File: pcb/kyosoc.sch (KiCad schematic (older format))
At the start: 134 parts, among them J1 USB_C_Receptacle, SW1 SW_Push, SW10 SW_Push, SW11 SW_Push, SW12 SW_Push, SW13 SW_Push, SW14 SW_Push, SW15 SW_Push, SW16 SW_Push, SW17 SW_Push, SW18 SW_Push, SW19 SW_Push, SW2 SW_Push, SW20 SW_Push, SW21 SW_Push, SW22 SW_Push, SW23 SW_Push, SW24 SW_Push, SW25 SW_Push, SW26 SW_Push, SW27 SW_Push, SW28 SW_Push, SW29 SW_Push, SW3 SW_Push, SW30 SW_Push, SW31 SW_Push, SW32 SW_Push, SW33 SW_Push, SW34 SW_Push, SW35 SW_Push, SW36 SW_Push, SW37 SW_Push, SW38 SW_Push, SW39 SW_Push, SW4 SW_Push, SW40 SW_Push, SW41 SW_Push, SW42 SW_Push, SW43 SW_Push, SW44 SW_Push, SW45 SW_Push, SW46 SW_Push, SW47 SW_Push, SW48 SW_Push, SW49 SW_Push, SW5 SW_Push, SW50 SW_Push, SW51 SW_Push, SW52 SW_Push, SW53 SW_Push, SW54 SW_Push, SW55 SW_Push, SW56 SW_Push, SW57 SW_Push, SW58 SW_Push, SW59 SW_Push, SW6 SW_Push, SW60 SW_Push, SW61 SW_Push, SW62 RESET, SW7 SW_Push, SW8 SW_Push, SW9 SW_Push, U1 ATmega32U4-AU, Y1 16MHz

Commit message: correspond to footprint (switches)
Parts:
- C1, C2: footprint (none) -> footprint:Kondensator-2.5mm
- SW1, SW10, SW11, SW12, SW13, SW14, SW15, SW16, SW17, SW18, SW19, SW2, SW20, SW21, SW22, SW23, SW24, SW25, SW26, SW27, SW28, SW29, SW3, SW30, SW31, SW32, SW33, SW34, SW35, SW36, SW37, SW38, SW39, SW4, SW40, SW41, SW42, SW43, SW44, SW45, SW46, SW47, SW48, SW49, SW5, SW50, SW51, SW52, SW53, SW54, SW55, SW56, SW57, SW58, SW59, SW6, SW60, SW61, SW7, SW8, SW9: footprint (none) -> footprint:Cherry-MX
- Y1: footprint (none) -> footprint:Crystal-HC-49-S

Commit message: add outer lines
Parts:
- U1: footprint Package_QFP:TQFP-44_10x10mm_P0.8mm -> footprint:TQFP44
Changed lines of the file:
@@
 F 0 "U1" H 5100 5300 50  0000 C CNN
 F 1 "ATmega32U4-AU" H 5100 5200 50  0000 C CNN
-F 2 "Package_QFP:TQFP-44_10x10mm_P0.8mm" H 5100 5250 50  0001 C CIN
+F 2 "footprint:TQFP44" H 5100 5250 50  0001 C CIN
 F 3 "http://ww1.microchip.com/downloads/en/DeviceDoc/Atmel-7766-8-bit-AVR-ATmega16U4-32U4_Datasheet.pdf" H 5100 5250 50  0001 C CNN
 	1    5100 5250

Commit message: update layout
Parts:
- D1, D10, D11, D12, D13, D14, D15, D16, D17, D18, D19, D2, D20, D21, D22, D23, D24, D25, D26, D27, D28, D29, D3, D30, D31, D32, D33, D34, D35, D36, D37, D38, D39, D4, D40, D41, D42, D43, D44, D45, D46, D47, D48, D49, D5, D50, D51, D52, D53, D54, D55, D56, D57, D58, D59, D6, D60, D61, D7, D8, D9: footprint (none) -> footprint:1N4148W
- J1: footprint (none) -> footprint:TYPE-C-31-M-12
- R1, R2, R3, R4, R5: footprint (none) -> footprint:Resistor
- SW1, SW10, SW11, SW12, SW13, SW14, SW15, SW16, SW17, SW18, SW19, SW2, SW20, SW21, SW22, SW23, SW24, SW25, SW26, SW27, SW28, SW29, SW3, SW30, SW31, SW32, SW33, SW34, SW35, SW36, SW37, SW38, SW39, SW4, SW40, SW41, SW42, SW43, SW44, SW45, SW46, SW47, SW48, SW49, SW5, SW50, SW51, SW52, SW53, SW54, SW55, SW56, SW57, SW58, SW59, SW6, SW60, SW61, SW7, SW8, SW9: footprint footprint:Cherry-MX -> footprint:Cherry-MX-Kailh-Socket
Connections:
- net D+: now also R4.1; no longer R3.1
- net D-: now also R3.1; no longer R4.1

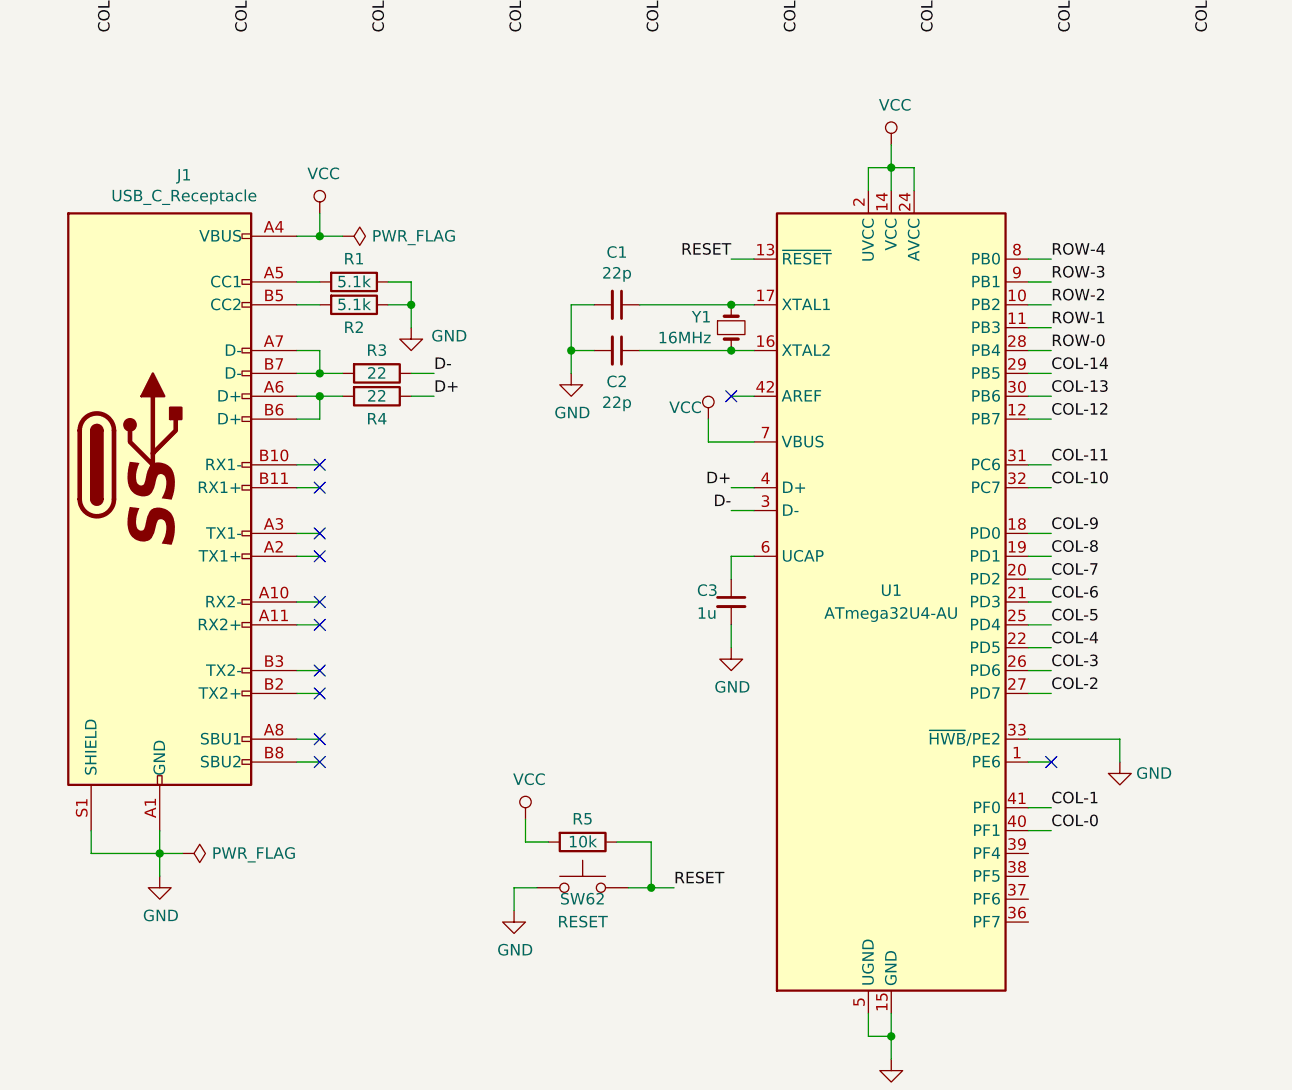
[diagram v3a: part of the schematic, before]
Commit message: wiring done without reset switch
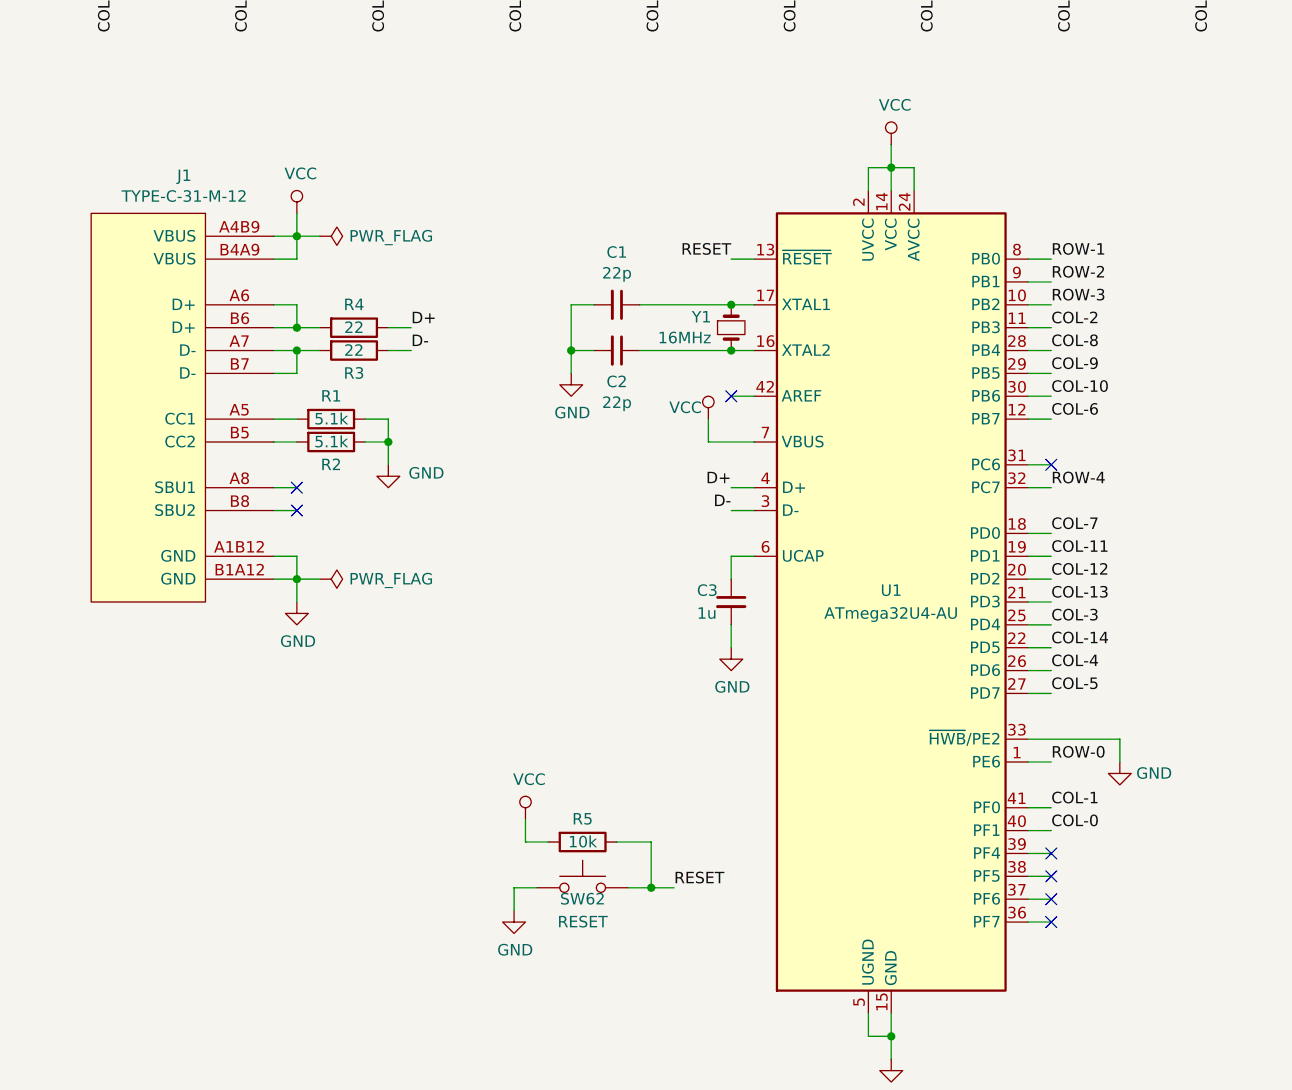
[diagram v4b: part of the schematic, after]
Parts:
- removed J1: USB_C_Receptacle, footprint:TYPE-C-31-M-12, symbol Connector:USB_C_Receptacle
- added J1: TYPE-C-31-M-12, footprint:TYPE-C-31-M-12, symbol kyosoc:TYPE-C-31-M-12
- C1, C2: footprint footprint:Kondensator-2.5mm -> footprint:1206-3216
- C3: footprint (none) -> footprint:1206-3216
- R1, R2, R3, R4, R5: footprint footprint:Resistor -> footprint:1206-3216
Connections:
- net COL-10: now also U1.30 (PB6); no longer U1.32 (PC7)
- net COL-11: now also U1.19 (PD1); no longer U1.31 (PC6)
- net COL-12: now also U1.20 (PD2); no longer U1.12 (PB7)
- net COL-13: now also U1.21 (PD3); no longer U1.30 (PB6)
- net COL-14: now also U1.22 (PD5); no longer U1.29 (PB5)
- net COL-2: now also U1.11 (PB3); no longer U1.27 (PD7)
- net COL-3: now also U1.25 (PD4); no longer U1.26 (PD6)
- net COL-4: now also U1.26 (PD6); no longer U1.22 (PD5)
- net COL-5: now also U1.27 (PD7); no longer U1.25 (PD4)
- net COL-6: now also U1.12 (PB7); no longer U1.21 (PD3)
- net COL-7: now also U1.18 (PD0); no longer U1.20 (PD2)
- net COL-8: now also U1.28 (PB4); no longer U1.19 (PD1)
- net COL-9: now also U1.29 (PB5); no longer U1.18 (PD0)
- net GND: now also J1.A1B12 (GND), J1.B1A12 (GND)
- net ROW-0: now also U1.1 (PE6); no longer U1.28 (PB4)
- net ROW-1: now also U1.8 (PB0); no longer U1.11 (PB3)
- net ROW-2: now also U1.9 (PB1); no longer U1.10 (PB2)
- net ROW-3: now also U1.10 (PB2); no longer U1.9 (PB1)
- net ROW-4: now also U1.32 (PC7); no longer U1.8 (PB0)
- net VCC: now also J1.A4B9 (VBUS), J1.B4A9 (VBUS)
- net at R1.2: now also J1.A5 (CC1)
- net at R4.2: now also J1.A6 (D+), J1.B6 (D+)
- net at R3.2: now also J1.A7 (D-), J1.B7 (D-)
- net at R2.2: now also J1.B5 (CC2)
- no-connect marks 12 -> 8
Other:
- moved on the sheet: R1, R2, R3, R4

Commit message: add tact-switch
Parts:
- added R6: 10k, footprint:1206-3216, symbol Device:R
- SW62: footprint (none) -> footprint:Tact-Switch
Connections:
- net GND: now also R6.1; no longer U1.33 (~HWB~/PE2)
- new net: R6.2, U1.33 (~HWB~/PE2)
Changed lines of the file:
@@
 Wire Wire Line
 	5100 3350 5200 3350
-$Comp
-L power:VCC #PWR01
-U 1 1 5E6C5CB4
-P 5100 3250
-F 0 "#PWR01" H 5100 3100 50  0001 C CNN
-F 1 "VCC" H 5117 3423 50  0000 C CNN
-F 2 "" H 5100 3250 50  0001 C CNN
-F 3 "" H 5100 3250 50  0001 C CNN
-	1    5100 3250
-	1    0    0    -1
-$EndComp
 Wire Wire Line
 	5100 3250 5100 3350
@@
 L power:GND #PWR07
 U 1 1 5E6C7FE0
-P 6100 5950
-F 0 "#PWR07" H 6100 5700 50  0001 C CNN
-F 1 "GND" H 6250 5900 50  0000 C CNN
-F 2 "" H 6100 5950 50  0001 C CNN
-F 3 "" H 6100 5950 50  0001 C CNN
-	1    6100 5950
-	1    0    0    -1
-$EndComp
-Wire Wire Line
-	6100 5850 6100 5950
+P 6200 5950
+F 0 "#PWR07" H 6200 5700 50  0001 C CNN
+F 1 "GND" H 6350 5900 50  0000 C CNN
+F 2 "" H 6200 5950 50  0001 C CNN
+F 3 "" H 6200 5950 50  0001 C CNN
+	1    6200 5950
+	1    0    0    -1
+$EndComp
+Wire Wire Line
+	6200 5850 6200 5950
 $Comp
 L Device:Crystal_Small Y1
@@
 $EndComp
 Wire Wire Line
-	2500 3650 2600 3650
-Connection ~ 2500 3650
-$Comp
-L power:PWR_FLAG #FLG01
-U 1 1 5E6E4D6F
-P 2600 3650
-F 0 "#FLG01" H 2600 3725 50  0001 C CNN
-F 1 "PWR_FLAG" V 2600 3778 50  0000 L CNN
-F 2 "" H 2600 3650 50  0001 C CNN
-F 3 "~" H 2600 3650 50  0001 C CNN
-	1    2600 3650
-	0    1    1    0
-$EndComp
-Wire Wire Line
 	2500 5050 2500 5150
 Connection ~ 2500 5150
@@
 	1    2500 5250
 	1    0    0    -1
-$EndComp
-Wire Wire Line
-	2500 5150 2600 5150
-$Comp
-L power:PWR_FLAG #FLG02
-U 1 1 5E6E8B43
-P 2600 5150
-F 0 "#FLG02" H 2600 5225 50  0001 C CNN
-F 1 "PWR_FLAG" V 2600 5278 50  0000 L CNN
-F 2 "" H 2600 5150 50  0001 C CNN
-F 3 "~" H 2600 5150 50  0001 C CNN
-	1    2600 5150
-	0    1    1    0
 $EndComp
 Wire Wire Line
@@
 F 0 "SW62" H 3750 6450 50  0000 C CNN
 F 1 "RESET" H 3750 6350 50  0000 C CNN
-F 2 "" H 3750 6700 50  0001 C CNN
+F 2 "footprint:Tact-Switch" H 3750 6700 50  0001 C CNN
 F 3 "~" H 3750 6700 50  0001 C CNN
 	1    3750 6500
@@
 	5700 5950 5800 5950
 Wire Wire Line
-	5700 5850 6100 5850
-Wire Wire Line
 	5700 6250 5800 6250
 Wire Wire Line
@@
 Wire Wire Line
 	2500 3950 2500 4050
-Wire Wire Line
-	2400 3750 2500 3750
-Wire Wire Line
-	2500 3750 2500 3650
 Wire Wire Line
 	2400 5050 2500 5050
@@
 	1    0    0    -1
 $EndComp
+$Comp
+L Device:R R6
+U 1 1 5ED6E0AA
+P 5950 5850
+F 0 "R6" V 5850 5850 50  0000 C CNN
+F 1 "10k" V 5950 5850 50  0000 C CNN
+F 2 "footprint:1206-3216" V 5880 5850 50  0001 C CNN
+F 3 "~" H 5950 5850 50  0001 C CNN
+	1    5950 5850
+	0    1    1    0
+$EndComp
+Wire Wire Line
+	5700 5850 5800 5850
+Wire Wire Line
+	6100 5850 6200 5850
+$Comp
+L power:VCC #PWR01
+U 1 1 5E6C5CB4
+P 5100 3250
+F 0 "#PWR01" H 5100 3100 50  0001 C CNN
+F 1 "VCC" H 5117 3423 50  0000 C CNN
+F 2 "" H 5100 3250 50  0001 C CNN
+F 3 "" H 5100 3250 50  0001 C CNN
+	1    5100 3250
+	1    0    0    -1
+$EndComp
+$Comp
+L power:VCC #PWR0101
+U 1 1 5EE8B385
+P 7000 3250
+F 0 "#PWR0101" H 7000 3100 50  0001 C CNN
+F 1 "VCC" H 7017 3423 50  0000 C CNN
+F 2 "" H 7000 3250 50  0001 C CNN
+F 3 "" H 7000 3250 50  0001 C CNN
+	1    7000 3250
+	1    0    0    -1
+$EndComp
+$Comp
+L power:PWR_FLAG #FLG0101
+U 1 1 5EE8D030
+P 7100 3350
+F 0 "#FLG0101" H 7100 3425 50  0001 C CNN
+F 1 "PWR_FLAG" V 7100 3478 50  0000 L CNN
+F 2 "" H 7100 3350 50  0001 C CNN
+F 3 "~" H 7100 3350 50  0001 C CNN
+	1    7100 3350
+	0    1    1    0
+$EndComp
+$Comp
+L power:GND #PWR0102
+U 1 1 5EE8E1A1
+P 7000 3550
+F 0 "#PWR0102" H 7000 3300 50  0001 C CNN
+F 1 "GND" H 7005 3377 50  0000 C CNN
+F 2 "" H 7000 3550 50  0001 C CNN
+F 3 "" H 7000 3550 50  0001 C CNN
+	1    7000 3550
+	1    0    0    -1
+$EndComp
+$Comp
+L power:PWR_FLAG #FLG0102
+U 1 1 5EE8F2D8
+P 7100 3450
+F 0 "#FLG0102" H 7100 3525 50  0001 C CNN
+F 1 "PWR_FLAG" V 7100 3578 50  0000 L CNN
+F 2 "" H 7100 3450 50  0001 C CNN
+F 3 "~" H 7100 3450 50  0001 C CNN
+	1    7100 3450
+	0    1    1    0
+$EndComp
+Wire Wire Line
+	7000 3250 7000 3350
+Wire Wire Line
+	7000 3350 7100 3350
+Wire Wire Line
+	7000 3550 7000 3450
+Wire Wire Line
+	7000 3450 7100 3450
+Wire Wire Line
+	2400 3750 2500 3750
+Connection ~ 2500 3650
+Wire Wire Line
+	2500 3750 2500 3650
 $EndSCHEMATC
